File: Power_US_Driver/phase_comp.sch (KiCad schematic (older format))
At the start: 4 parts

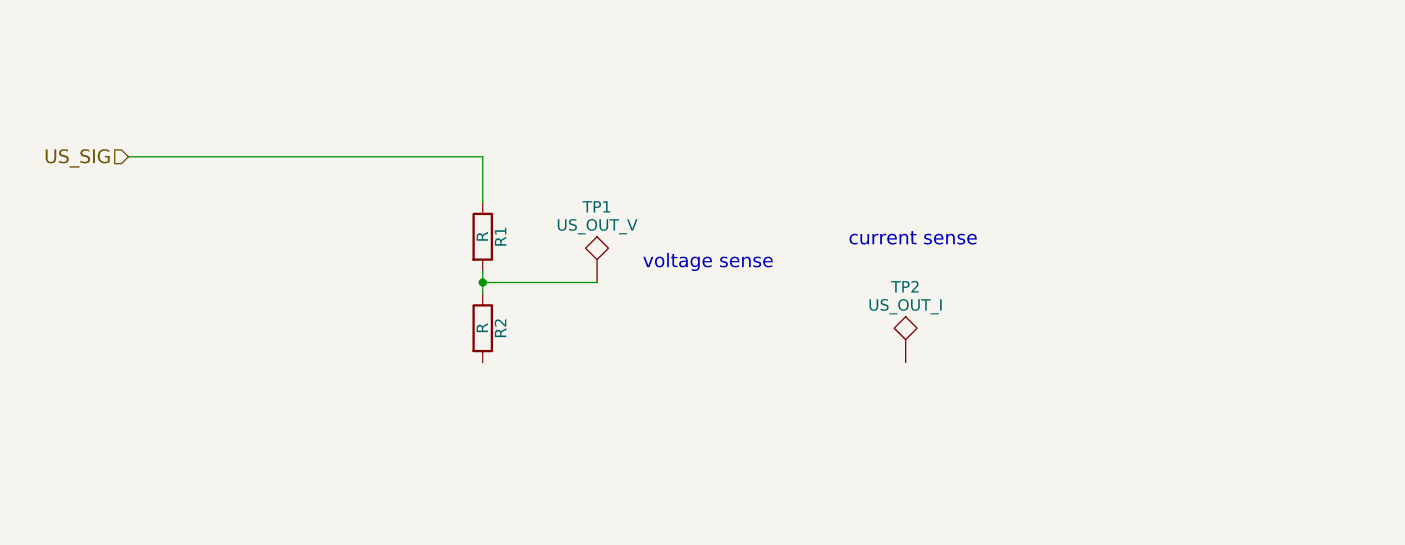
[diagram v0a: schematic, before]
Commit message: CURRENT SENSE REROUT, HIGHSIDE DRIVER GROUNDING
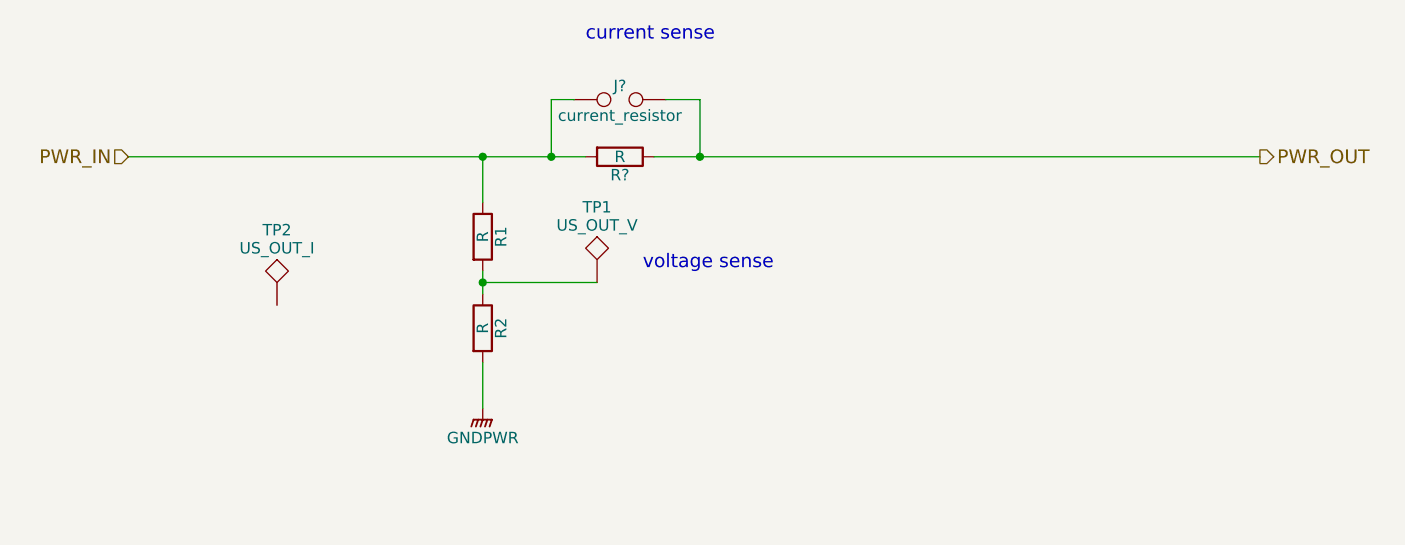
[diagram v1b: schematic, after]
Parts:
- added J?: current_resistor, symbol TEST_2P
- added R?: R, symbol R
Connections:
- net GNDPWR: now reaches R2.2
- net US_SIG renamed PWR_IN
- net PWR_IN: now also J?.1, R?.2
- new net PWR_OUT: J?.2, R?.1
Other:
- moved on the sheet: TP2
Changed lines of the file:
@@
 LIBS:LIA-cache
 LIBS:power_US
+LIBS:JasMoH_Parts
 LIBS:Power_US_Driver-cache
 EELAYER 25 0
@@
 Comment4 ""
 $EndDescr
-Text HLabel 1500 2650 0    60   Input ~ 0
-US_SIG
 $Comp
 L R R1
@@
 	3050 2850 3050 2650
 Wire Wire Line
-	3050 2650 1500 2650
+	1500 2650 3500 2650
 Wire Wire Line
 	3050 3150 3050 3250
 Text Notes 3750 3150 0    60   ~ 0
 voltage sense
-Text Notes 4650 3050 0    60   ~ 0
+Text Notes 3500 2150 0    60   ~ 0
 current sense
 $Comp
@@
 L TEST TP2
 U 1 1 5AAE8351
-P 4900 3550
-F 0 "TP2" H 4900 3850 50  0000 C BNN
-F 1 "US_OUT_I" H 4900 3800 50  0000 C CNN
-F 2 "" H 4900 3550 50  0001 C CNN
-F 3 "" H 4900 3550 50  0001 C CNN
-	1    4900 3550
+P 2150 3300
+F 0 "TP2" H 2150 3600 50  0000 C BNN
+F 1 "US_OUT_I" H 2150 3550 50  0000 C CNN
+F 2 "" H 2150 3300 50  0001 C CNN
+F 3 "" H 2150 3300 50  0001 C CNN
+	1    2150 3300
 	1    0    0    -1
 $EndComp
@@
 	3550 3200 3050 3200
 Connection ~ 3050 3200
+$Comp
+L GNDPWR #PWR?
+U 1 1 5AB1E2C1
+P 3050 3750
+F 0 "#PWR?" H 3050 3550 50  0001 C CNN
+F 1 "GNDPWR" H 3050 3620 50  0000 C CNN
+F 2 "" H 3050 3700 50  0001 C CNN
+F 3 "" H 3050 3700 50  0001 C CNN
+	1    3050 3750
+	1    0    0    -1
+$EndComp
+Wire Wire Line
+	3050 3750 3050 3550
+$Comp
+L TEST_2P J?
+U 1 1 5AB1E44D
+P 3650 2400
+F 0 "J?" H 3650 2460 50  0000 C CNN
+F 1 "current_resistor" H 3650 2330 50  0000 C CNN
+F 2 "" H 3650 2400 50  0001 C CNN
+F 3 "" H 3650 2400 50  0001 C CNN
+	1    3650 2400
+	1    0    0    -1
+$EndComp
+$Comp
+L R R?
+U 1 1 5AB1E48D
+P 3650 2650
+F 0 "R?" V 3730 2650 50  0000 C CNN
+F 1 "R" V 3650 2650 50  0000 C CNN
+F 2 "" V 3580 2650 50  0001 C CNN
+F 3 "" H 3650 2650 50  0001 C CNN
+	1    3650 2650
+	0    1    1    0
+$EndComp
+Connection ~ 3050 2650
+Wire Wire Line
+	3800 2650 6450 2650
+Wire Wire Line
+	4000 2650 4000 2400
+Wire Wire Line
+	4000 2400 3850 2400
+Wire Wire Line
+	3450 2400 3350 2400
+Wire Wire Line
+	3350 2400 3350 2650
+Connection ~ 3350 2650
+Text HLabel 6450 2650 2    60   Output ~ 0
+PWR_OUT
+Text HLabel 1500 2650 0    60   Input ~ 0
+PWR_IN
+Connection ~ 4000 2650
 $EndSCHEMATC

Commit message: initial Current sense more vacilating over power drive solution
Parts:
- removed J?: current_resistor, symbol TEST_2P
- removed R?: R, symbol R
- added U?: ACS711, symbol ACS711
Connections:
- net PWR_IN: now also U?.3 (IP-), U?.4 (IP-); no longer R1.1
- net PWR_OUT: now also R1.1, U?.1 (IP+), U?.2 (IP+)
- net Vsense: now reaches R1.2, R2.1, TP1.1
- net Viout: now reaches TP2.1
- net Viout: now also U?.7 (VIout)
- new net 5v: U?.8 (Vcc)
- new net GNDD: U?.5 (GND)
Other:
- moved on the sheet: TP2
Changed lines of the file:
@@
 	3050 2850 3050 2650
-Wire Wire Line
-	1500 2650 3500 2650
 Wire Wire Line
 	3050 3150 3050 3250
@@
 L TEST TP2
 U 1 1 5AAE8351
-P 2150 3300
-F 0 "TP2" H 2150 3600 50  0000 C BNN
-F 1 "US_OUT_I" H 2150 3550 50  0000 C CNN
-F 2 "" H 2150 3300 50  0001 C CNN
-F 3 "" H 2150 3300 50  0001 C CNN
-	1    2150 3300
+P 4900 3550
+F 0 "TP2" H 4900 3850 50  0000 C BNN
+F 1 "US_OUT_I" H 4900 3800 50  0000 C CNN
+F 2 "" H 4900 3550 50  0001 C CNN
+F 3 "" H 4900 3550 50  0001 C CNN
+	1    4900 3550
 	1    0    0    -1
 $EndComp
 Wire Wire Line
-	3550 3200 3050 3200
+	3050 3200 6450 3200
 Connection ~ 3050 3200
 $Comp
-L GNDPWR #PWR?
+L GNDPWR #PWR10
 U 1 1 5AB1E2C1
 P 3050 3750
-F 0 "#PWR?" H 3050 3550 50  0001 C CNN
+F 0 "#PWR10" H 3050 3550 50  0001 C CNN
 F 1 "GNDPWR" H 3050 3620 50  0000 C CNN
 F 2 "" H 3050 3700 50  0001 C CNN
@@
 Wire Wire Line
 	3050 3750 3050 3550
-$Comp
-L TEST_2P J?
-U 1 1 5AB1E44D
-P 3650 2400
-F 0 "J?" H 3650 2460 50  0000 C CNN
-F 1 "current_resistor" H 3650 2330 50  0000 C CNN
-F 2 "" H 3650 2400 50  0001 C CNN
-F 3 "" H 3650 2400 50  0001 C CNN
-	1    3650 2400
-	1    0    0    -1
-$EndComp
-$Comp
-L R R?
-U 1 1 5AB1E48D
-P 3650 2650
-F 0 "R?" V 3730 2650 50  0000 C CNN
-F 1 "R" V 3650 2650 50  0000 C CNN
-F 2 "" V 3580 2650 50  0001 C CNN
-F 3 "" H 3650 2650 50  0001 C CNN
-	1    3650 2650
-	0    1    1    0
-$EndComp
 Connection ~ 3050 2650
-Wire Wire Line
-	3800 2650 6450 2650
-Wire Wire Line
-	4000 2650 4000 2400
-Wire Wire Line
-	4000 2400 3850 2400
-Wire Wire Line
-	3450 2400 3350 2400
-Wire Wire Line
-	3350 2400 3350 2650
-Connection ~ 3350 2650
 Text HLabel 6450 2650 2    60   Output ~ 0
 PWR_OUT
 Text HLabel 1500 2650 0    60   Input ~ 0
 PWR_IN
-Connection ~ 4000 2650
+$Comp
+L ACS711 U?
+U 1 1 5AB2A81A
+P 2300 3000
+F 0 "U?" H 2200 3400 60  0000 C CNN
+F 1 "ACS711" H 2300 2800 60  0000 C CNN
+F 2 "" H 2300 3000 60  0001 C CNN
+F 3 "" H 2300 3000 60  0001 C CNN
+	1    2300 3000
+	0    1    1    0
+$EndComp
+Wire Wire Line
+	1500 2650 2350 2650
+Connection ~ 2250 2650
+Wire Wire Line
+	2450 2650 6450 2650
+Connection ~ 2550 2650
+$Comp
+L GNDD #PWR?
+U 1 1 5AB2AA31
+P 2250 3700
+F 0 "#PWR?" H 2250 3450 50  0001 C CNN
+F 1 "GNDD" H 2250 3575 50  0000 C CNN
+F 2 "" H 2250 3700 50  0001 C CNN
+F 3 "" H 2250 3700 50  0001 C CNN
+	1    2250 3700
+	1    0    0    -1
+$EndComp
+Wire Wire Line
+	2250 3700 2250 3500
+Text HLabel 1450 3650 0    60   Input ~ 0
+5v
+Wire Wire Line
+	1450 3650 2550 3650
+Wire Wire Line
+	2550 3650 2550 3500
+Text HLabel 6450 3550 2    60   Output ~ 0
+Viout
+Wire Wire Line
+	6450 3550 2450 3550
+Wire Wire Line
+	2450 3550 2450 3500
+Connection ~ 4900 3550
+Text HLabel 6450 3200 2    60   Output ~ 0
+Vsense
+Connection ~ 3550 3200
 $EndSCHEMATC

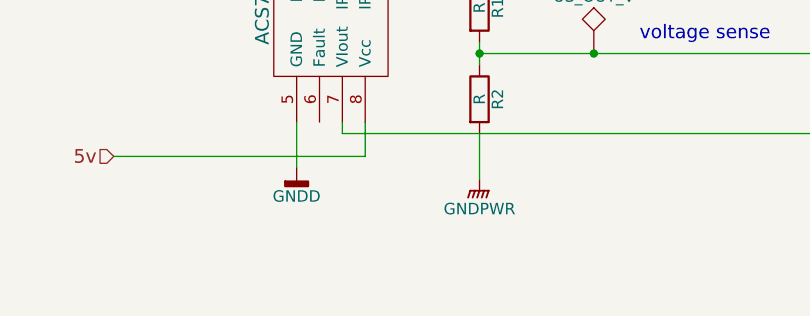
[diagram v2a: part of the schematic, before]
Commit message: Parts library creation
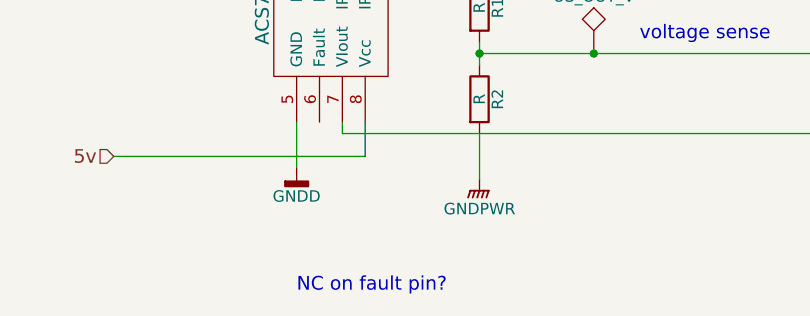
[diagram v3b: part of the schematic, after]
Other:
- note added: "NC on fault pin?"
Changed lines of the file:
@@
 Vsense
 Connection ~ 3550 3200
+Text Notes 2250 4250 0    60   ~ 0
+NC on fault pin?
 $EndSCHEMATC

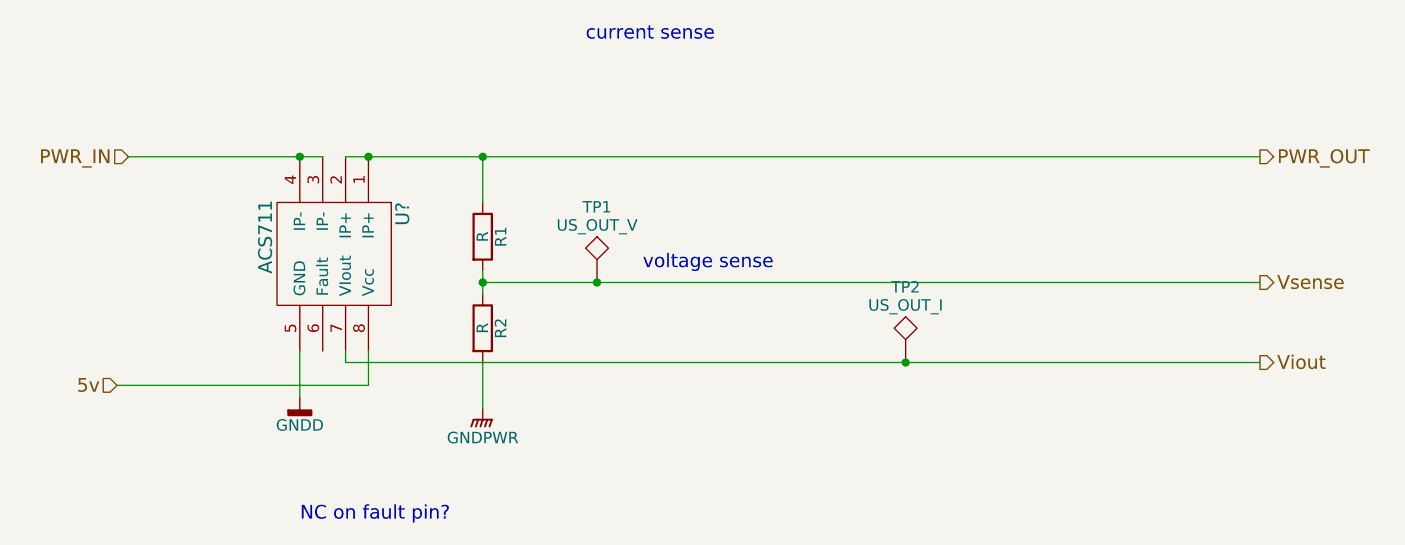
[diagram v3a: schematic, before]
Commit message: moved high current diode off board
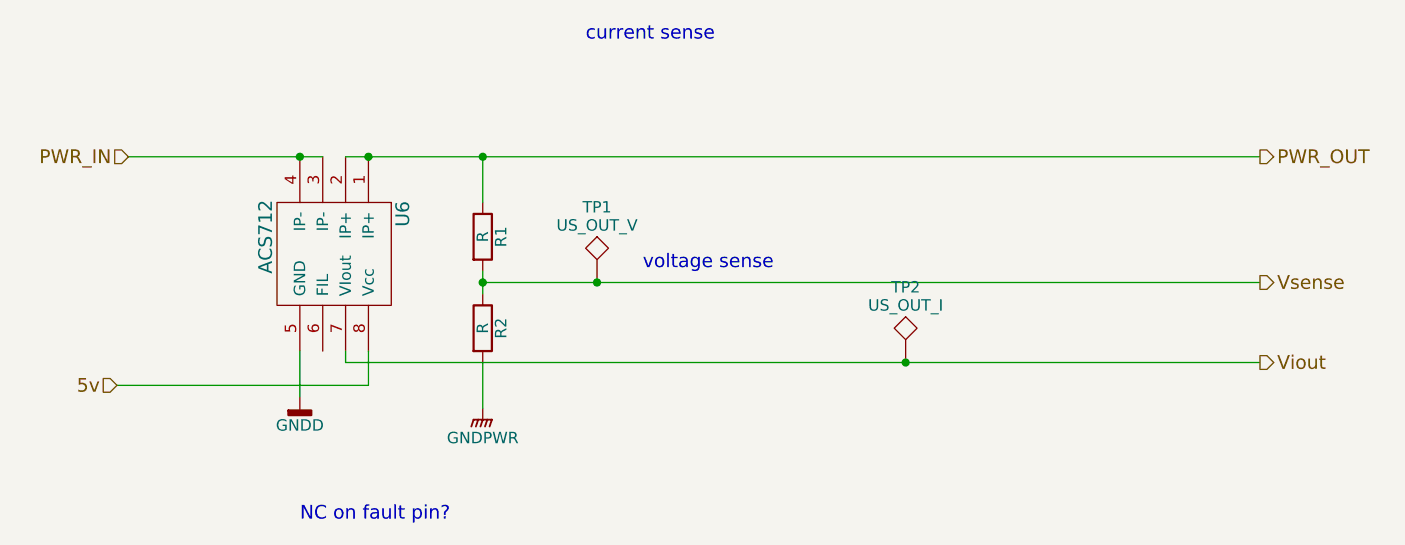
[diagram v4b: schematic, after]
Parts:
- removed U?: ACS711, symbol ACS711
- added U6: ACS712, symbol ACS712
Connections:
- net 5v: now also U6.8 (Vcc)
- net GNDD: now also U6.5 (GND)
- net PWR_IN: now also U6.3 (IP-), U6.4 (IP-)
- net PWR_OUT: now also U6.1 (IP+), U6.2 (IP+)
- net Viout: now also U6.7 (VIout)
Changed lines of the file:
@@
 Connection ~ 3050 3200
 $Comp
-L GNDPWR #PWR10
+L GNDPWR #PWR010
 U 1 1 5AB1E2C1
 P 3050 3750
-F 0 "#PWR10" H 3050 3550 50  0001 C CNN
+F 0 "#PWR010" H 3050 3550 50  0001 C CNN
 F 1 "GNDPWR" H 3050 3620 50  0000 C CNN
 F 2 "" H 3050 3700 50  0001 C CNN
@@
 Text HLabel 1500 2650 0    60   Input ~ 0
 PWR_IN
-$Comp
-L ACS711 U?
-U 1 1 5AB2A81A
-P 2300 3000
-F 0 "U?" H 2200 3400 60  0000 C CNN
-F 1 "ACS711" H 2300 2800 60  0000 C CNN
-F 2 "" H 2300 3000 60  0001 C CNN
-F 3 "" H 2300 3000 60  0001 C CNN
-	1    2300 3000
-	0    1    1    0
-$EndComp
 Wire Wire Line
 	1500 2650 2350 2650
@@
 Connection ~ 2550 2650
 $Comp
-L GNDD #PWR?
+L GNDD #PWR011
 U 1 1 5AB2AA31
 P 2250 3700
-F 0 "#PWR?" H 2250 3450 50  0001 C CNN
+F 0 "#PWR011" H 2250 3450 50  0001 C CNN
 F 1 "GNDD" H 2250 3575 50  0000 C CNN
 F 2 "" H 2250 3700 50  0001 C CNN
@@
 Text Notes 2250 4250 0    60   ~ 0
 NC on fault pin?
+$Comp
+L ACS712 U6
+U 1 1 5AB2D03C
+P 2300 3000
+F 0 "U6" H 2200 3400 60  0000 C CNN
+F 1 "ACS712" H 2300 2800 60  0000 C CNN
+F 2 "" H 2300 3000 60  0001 C CNN
+F 3 "" H 2300 3000 60  0001 C CNN
+	1    2300 3000
+	0    1    1    0
+$EndComp
 $EndSCHEMATC
